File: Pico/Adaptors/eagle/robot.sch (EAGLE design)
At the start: 23 parts, among them J1 JST-2P-SMD-PW-3410050P1, U1 HC_05

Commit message: todo
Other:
- note added: "TODO: IR remote control? Bring out other IOs?"
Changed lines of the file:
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@@
 <text x="78.74" y="40.64" size="1.778" layer="91">GPIO2</text>
 <text x="71.12" y="-2.54" size="1.778" layer="91">Farnell 1759435</text>
+<text x="68.58" y="-17.78" size="1.778" layer="91">TODO:
+IR remote control?
+Bring out other IOs?</text>
 </plain>
 <instances>

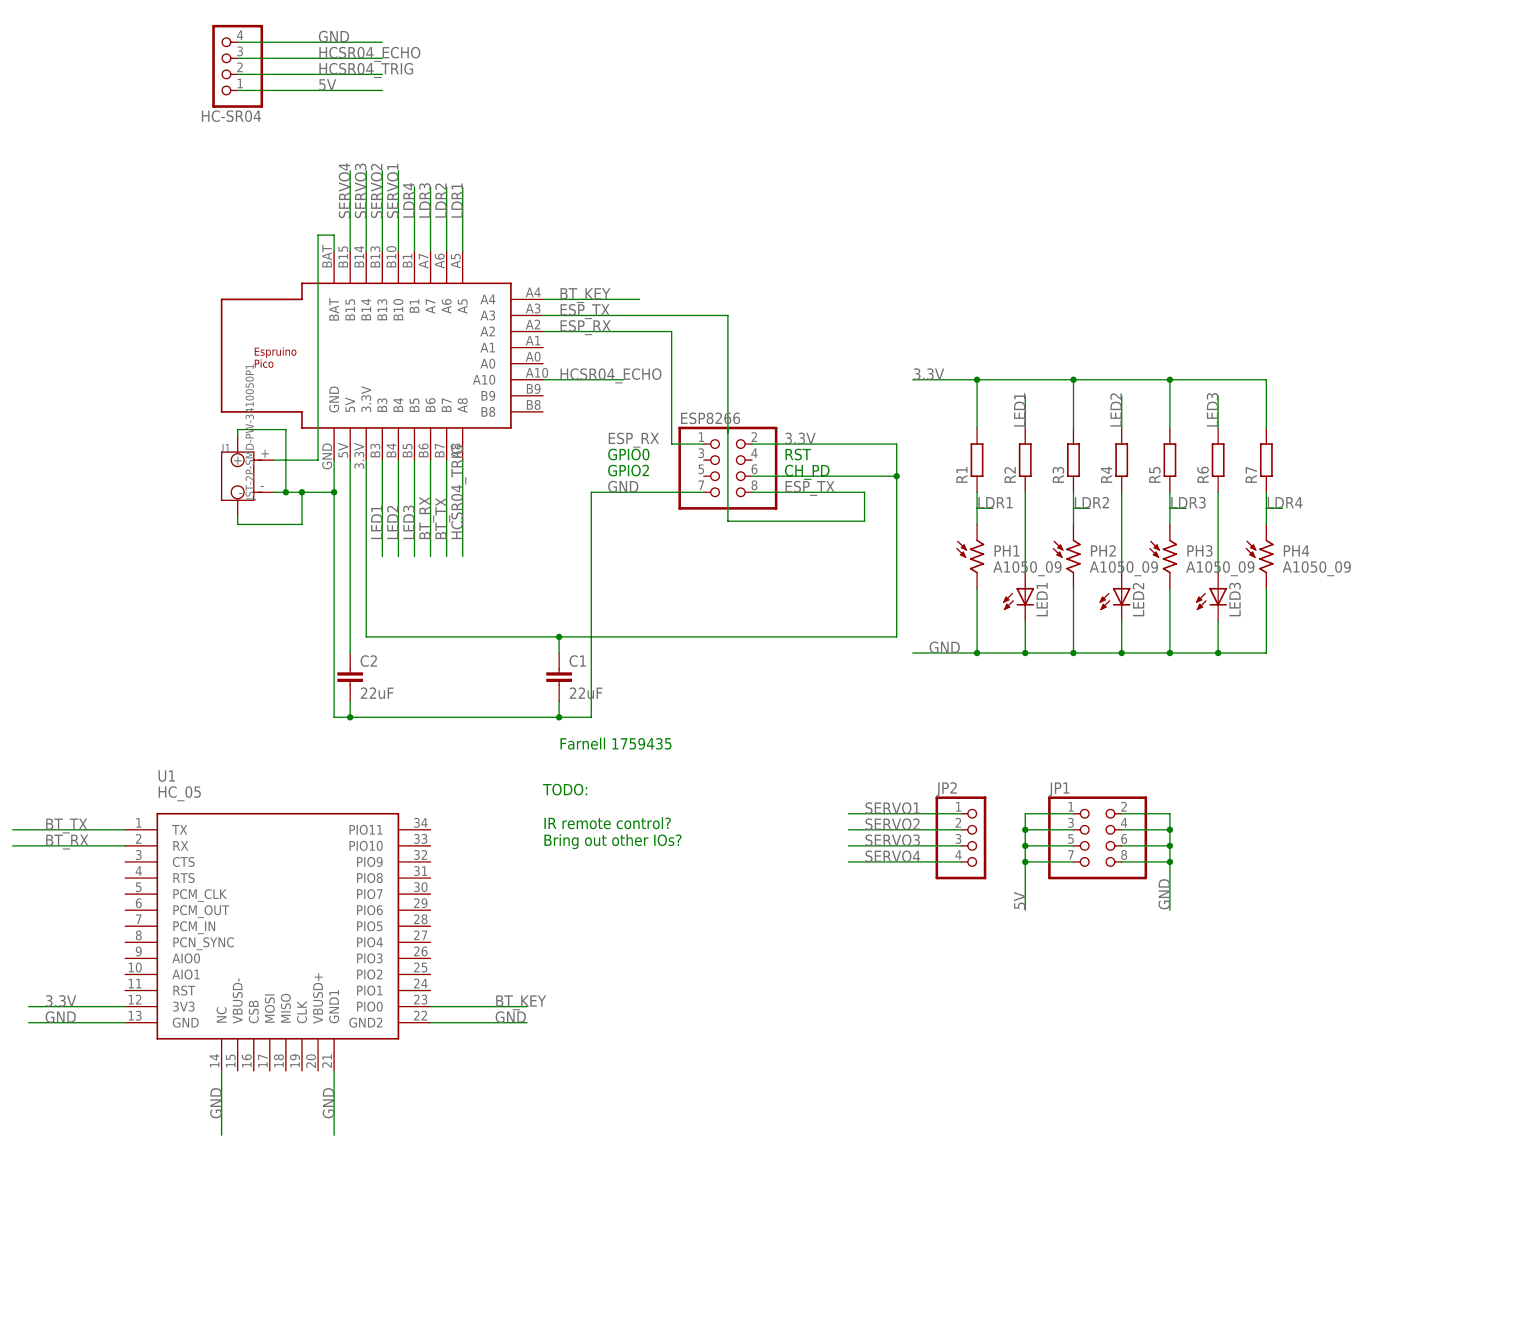
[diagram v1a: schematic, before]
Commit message: added another ultrasonic sensor, pins down the side, and ADNS5050 optical sensor
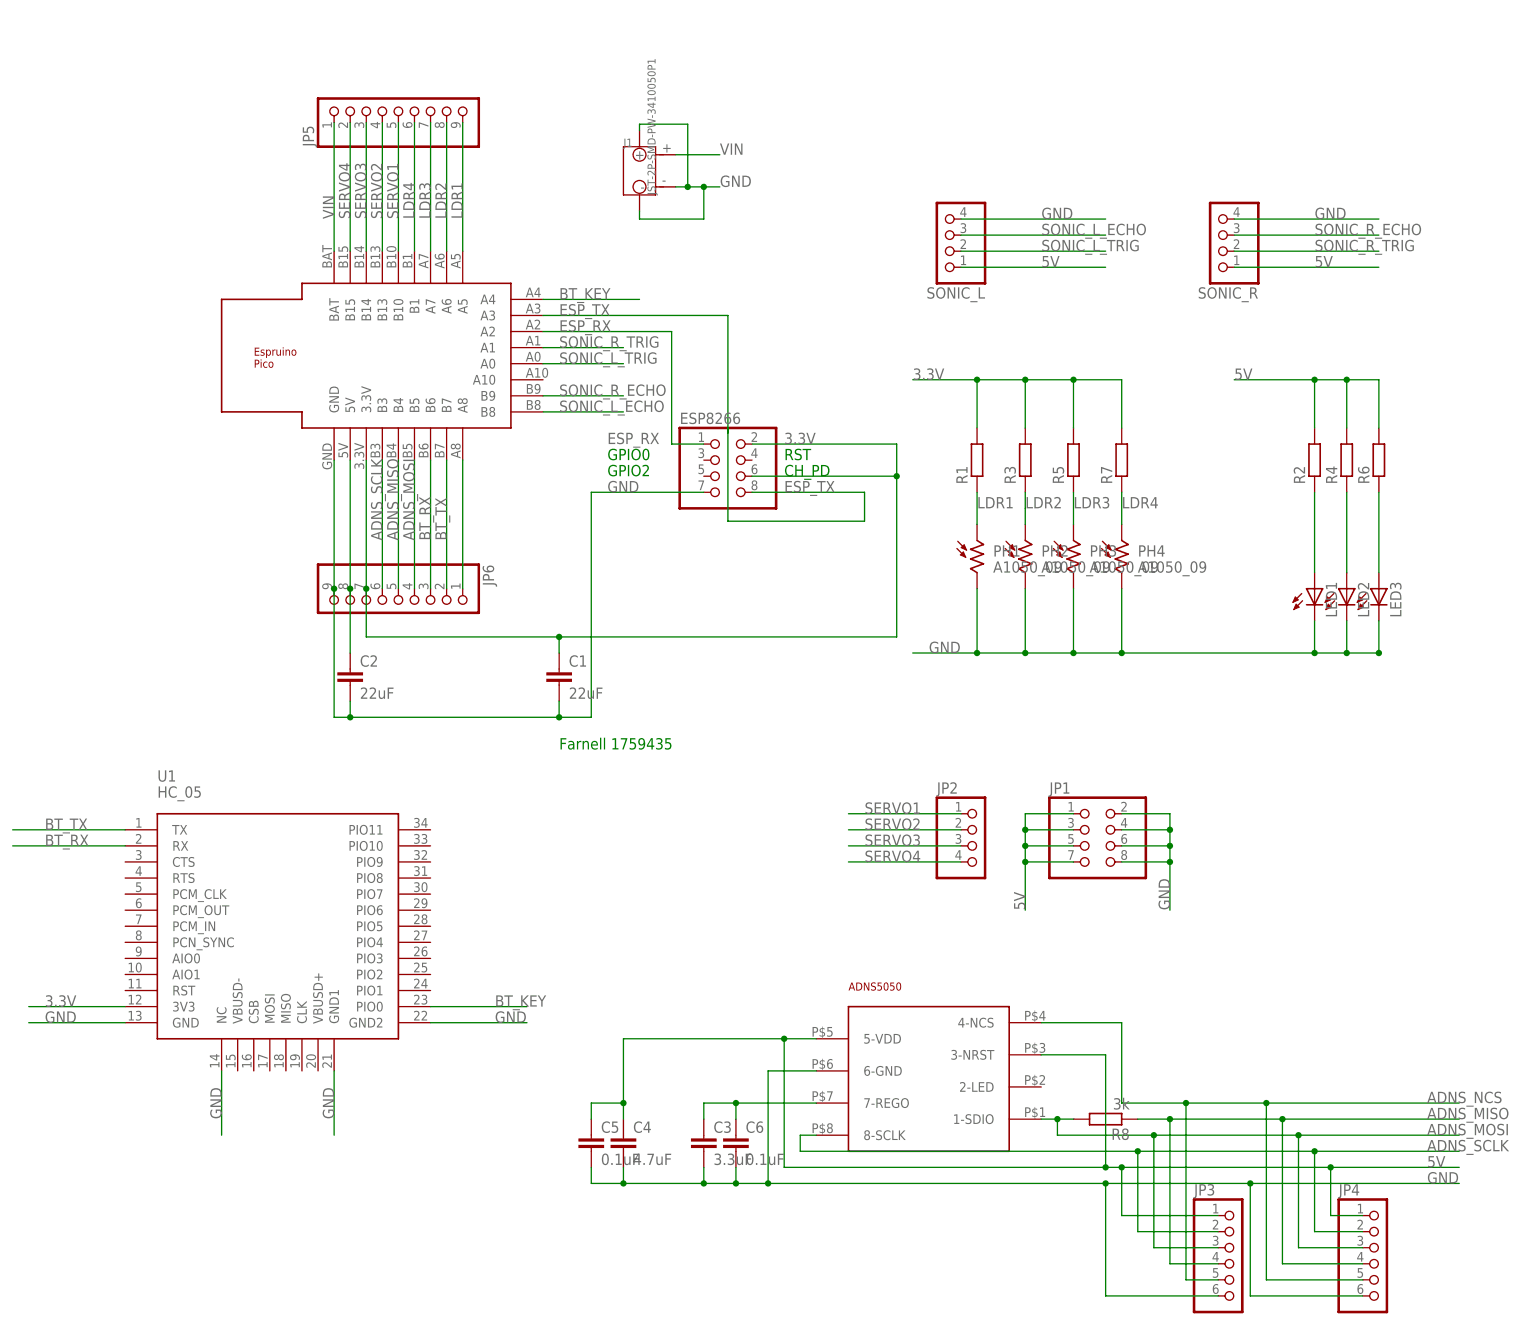
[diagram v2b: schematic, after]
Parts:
- removed HC-SR04: (no value), pinhead:PINHD-1X4
- added C3: 3.3uF, rcl:C-EUC1206
- added C4: 4.7uF, rcl:C-EUC1206
- added C5, C6: 0.1uF, rcl:C-EUC1206
- added JP3, JP4: (no value), pinhead:PINHD-1X6
- added JP5, JP6: (no value), pinhead:PINHD-1X9
- added R8: 3k, rcl:R-EU_R1206
- added SONIC_L, SONIC_R: (no value), pinhead:PINHD-1X4
- added U$2: ADNS5050, adns5050:ADNS5050
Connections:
- removed net HCSR04_ECHO: HC-SR04.3, U$1.A10
- removed net HCSR04_TRIG: HC-SR04.2, U$1.A8
- removed net LED1: R2.2, U$1.B3
- removed net LED2: R4.2, U$1.B4
- removed net LED3: R6.2, U$1.B5
- new net ADNS_MISO: JP3.4, JP4.4, JP6.5, R8.1, U$1.B4
- new net ADNS_MOSI: JP3.3, JP4.3, JP6.4, R8.2, U$1.B5, U$2.1-SDIO
- new net ADNS_NCS: JP3.5, JP4.5, U$2.4-NCS
- new net ADNS_SCLK: JP3.2, JP4.2, JP6.6, U$1.B3, U$2.8-SCLK
- new net N$1: JP6.1, U$1.A8
- new net N$2: C3.1, C6.1, U$2.7-REGO
- new net SONIC_L_ECHO: SONIC_L.3, U$1.B8
- new net SONIC_L_TRIG: SONIC_L.2, U$1.A0
- new net SONIC_R_ECHO: SONIC_R.3, U$1.B9
- new net SONIC_R_TRIG: SONIC_R.2, U$1.A1
- net 3.3V: now also JP6.7
- net 5V: now also C4.1, C5.1, JP3.1, JP4.1, JP6.8, R2.2, R4.2, R6.2, SONIC_L.1, SONIC_R.1, U$2.3-NRST, U$2.5-VDD; no longer HC-SR04.1
- net BT_RX: now also JP6.3
- net BT_TX: now also JP6.2
- net GND: now also C3.2, C4.2, C5.2, C6.2, JP3.6, JP4.6, JP6.9, SONIC_L.4, SONIC_R.4, U$2.6-GND; no longer HC-SR04.4
- net LDR1: now also JP5.9
- net LDR2: now also JP5.8
- net LDR3: now also JP5.7
- net LDR4: now also JP5.6
- net SERVO1: now also JP5.5
- net SERVO2: now also JP5.4
- net SERVO3: now also JP5.3
- net SERVO4: now also JP5.2
- net VIN: now also JP5.1
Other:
- note removed: "TODO: IR remote control? Bring out other IOs?"
- moved on the sheet: J1, LED1, LED2, LED3, PH2, PH3, PH4, R2, R3, R4, R5, R6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

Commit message: misc tweaks
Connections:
- net ADNS_NCS: now also U$1.A10
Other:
- moved on the sheet: C3, C4, C5, C6, JP1, JP2, JP3, JP4, R8
